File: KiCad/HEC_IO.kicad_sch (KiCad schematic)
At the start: 22 parts, among them SW1 SW_DIP_x04, U12 74LS04, U17 74LS20, U22 74LS02, U30 74LS74, U31 74LS32, U32 LM79M05_TO220, U33 74LS20, U34 74LS393, U35 74LS08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

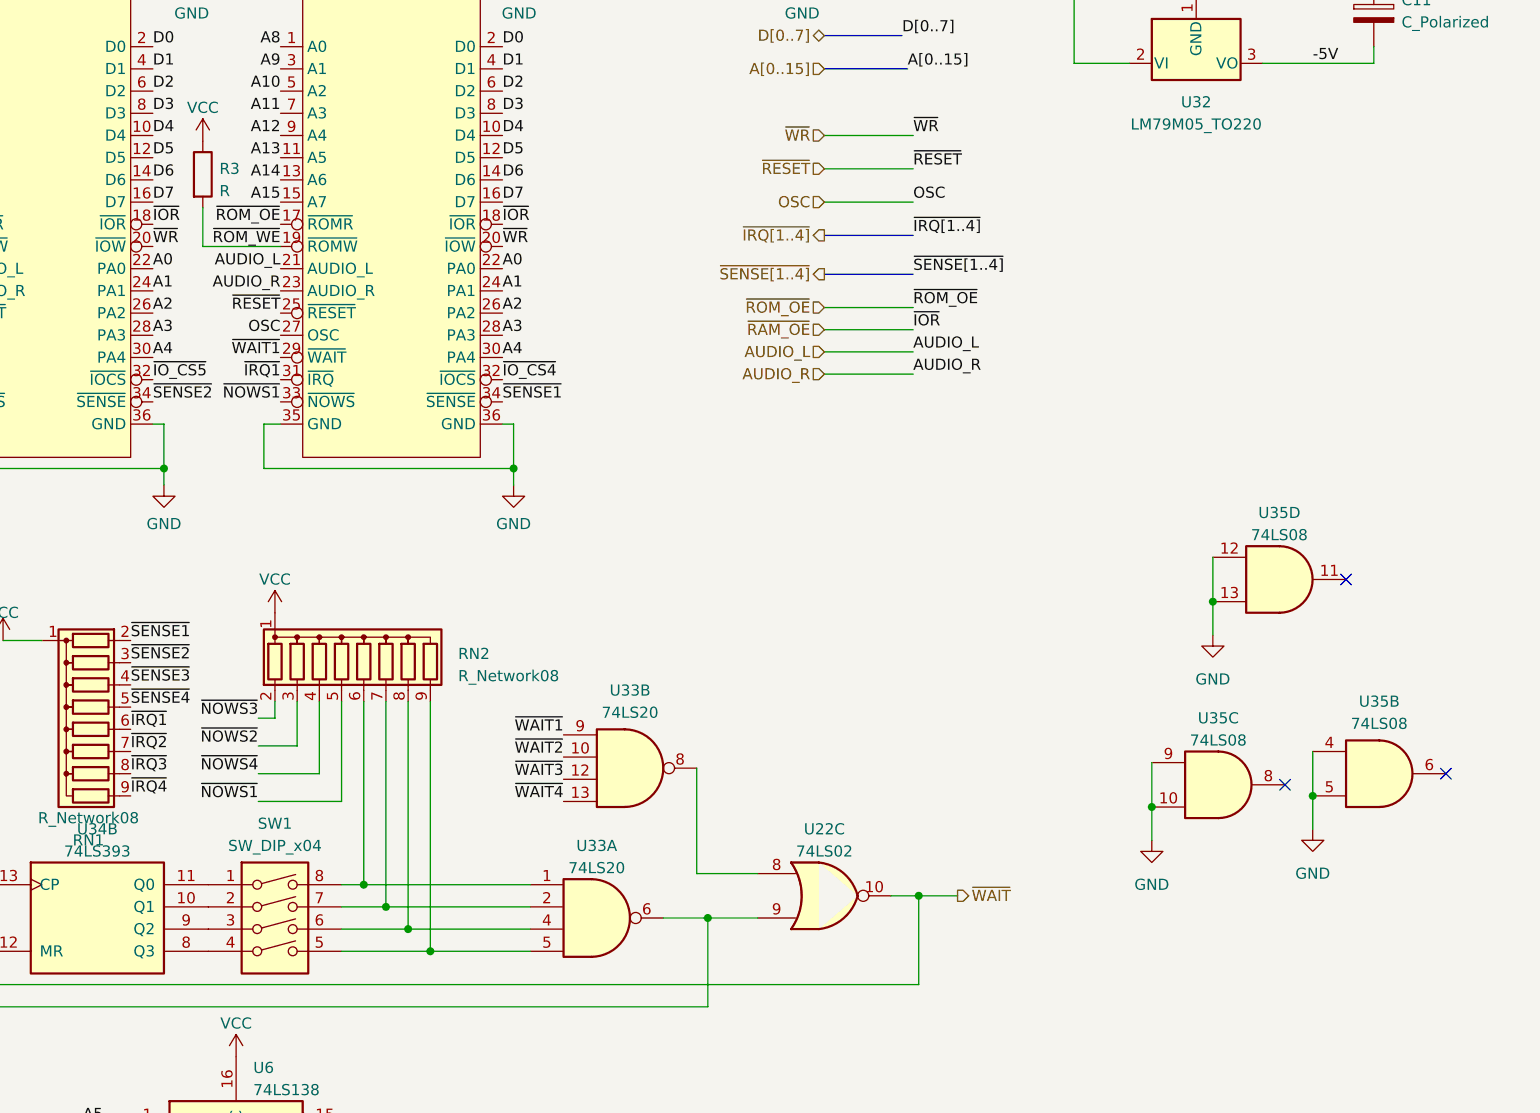
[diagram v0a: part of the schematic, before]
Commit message: Exchange RI and NX pins on bus driver
A mistake is found in the schematic: the RI and NX bits are exchanged on the 74245 bus driver chip. The mistake has been corrected. This change is significant since it changes the (non-existent) software programming model. More playing around with the layout.
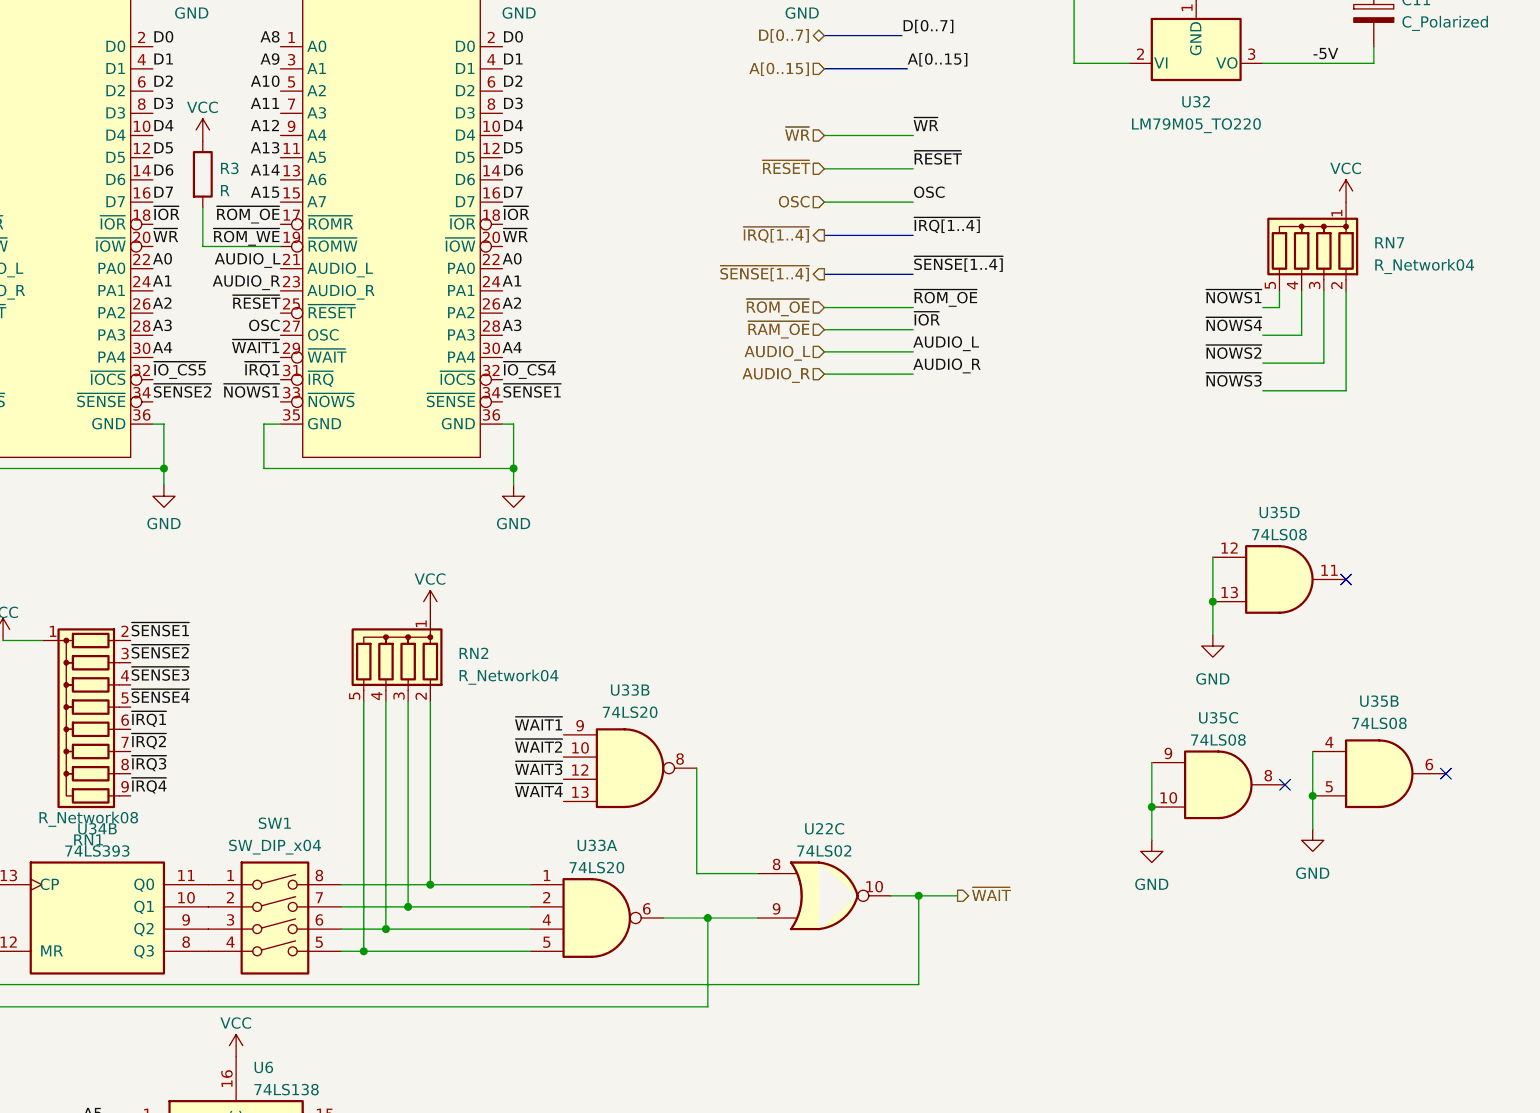
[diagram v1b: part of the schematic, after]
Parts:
- removed RN2: R_Network08, Resistor_THT:R_Array_SIP9, symbol Device:R_Network08
- added RN2, RN7: R_Network04, Resistor_THT:R_Array_SIP5, symbol Device:R_Network04
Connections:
- net VCC: now also RN2.1 (common), RN7.1 (common)
- net ~{NOWS1}: now also RN7.5 (R4)
- net ~{NOWS2}: now also RN7.3 (R2)
- net ~{NOWS3}: now also RN7.2 (R1)
- net ~{NOWS4}: now also RN7.4 (R3)
- net at SW1.5, U33.5: now also RN2.5 (R4)
- net at SW1.6, U33.4: now also RN2.4 (R3)
- net at SW1.7, U33.2: now also RN2.3 (R2)
- net at SW1.8, U33.1: now also RN2.2 (R1)

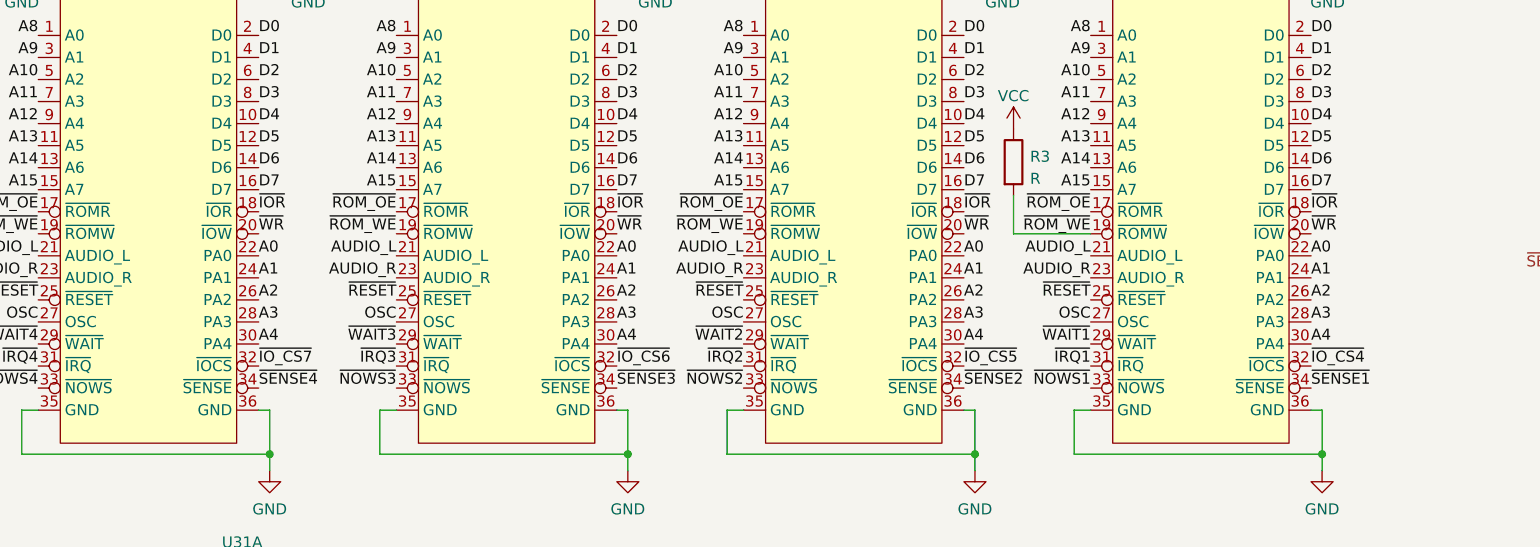
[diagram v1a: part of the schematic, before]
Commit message: Update to bus pinout
Move /RD and /WR signal closer to /CS to simplify add-on card design for common chips. From a simple search of pinouts of common chips this may reduce the amount of vias needed on the card.
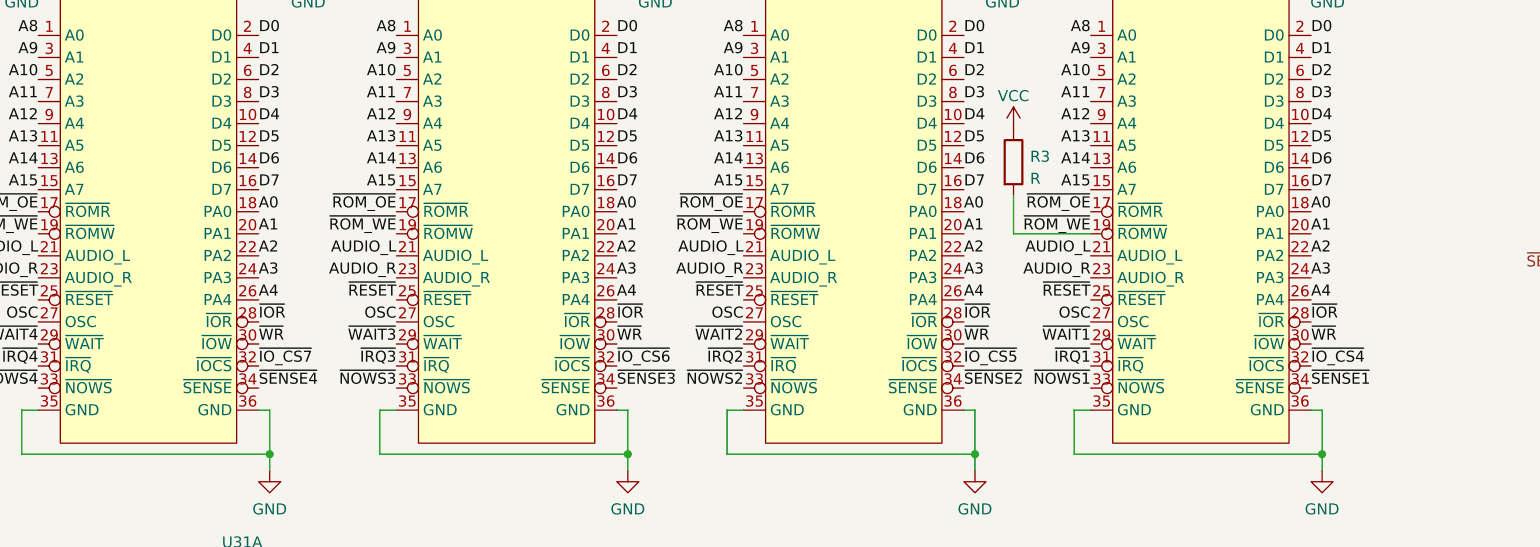
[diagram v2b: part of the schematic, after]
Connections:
- net A0: now also BUS1.18 (PA0), BUS2.18 (PA0), BUS3.18 (PA0), BUS4.18 (PA0); no longer BUS1.22 (PA0), BUS2.22 (PA0), BUS3.22 (PA0), BUS4.22 (PA0)
- net A1: now also BUS1.20 (PA1), BUS2.20 (PA1), BUS3.20 (PA1), BUS4.20 (PA1); no longer BUS1.24 (PA1), BUS2.24 (PA1), BUS3.24 (PA1), BUS4.24 (PA1)
- net A2: now also BUS1.22 (PA2), BUS2.22 (PA2), BUS3.22 (PA2), BUS4.22 (PA2); no longer BUS1.26 (PA2), BUS2.26 (PA2), BUS3.26 (PA2), BUS4.26 (PA2)
- net A3: now also BUS1.24 (PA3), BUS2.24 (PA3), BUS3.24 (PA3), BUS4.24 (PA3); no longer BUS1.28 (PA3), BUS2.28 (PA3), BUS3.28 (PA3), BUS4.28 (PA3)
- net A4: now also BUS1.26 (PA4), BUS2.26 (PA4), BUS3.26 (PA4), BUS4.26 (PA4); no longer BUS1.30 (PA4), BUS2.30 (PA4), BUS3.30 (PA4), BUS4.30 (PA4)
- net ~{RAM_OE}: now also BUS1.28 (~{IOR}), BUS2.28 (~{IOR}), BUS3.28 (~{IOR}), BUS4.28 (~{IOR}); no longer BUS1.18 (~{IOR}), BUS2.18 (~{IOR}), BUS3.18 (~{IOR}), BUS4.18 (~{IOR})
- net ~{WR}: now also BUS1.30 (~{IOW}), BUS2.30 (~{IOW}), BUS3.30 (~{IOW}), BUS4.30 (~{IOW}); no longer BUS1.20 (~{IOW}), BUS2.20 (~{IOW}), BUS3.20 (~{IOW}), BUS4.20 (~{IOW})

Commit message: Bug fixes
fixed some bugs introduced to the schematic. More routing.
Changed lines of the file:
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@@
-    (effects (font (size 1.27 1.27)) (justify right bottom))
-  )
-  (label "~{IORQ}" (at 123.19 181.61 180) (fields_autoplaced)
     (effects (font (size 1.27 1.27)) (justify right bottom))
   )
@@
     (effects (font (size 1.27 1.27)) (justify right))
   )
+  (hierarchical_label "~{IORQ}" (shape input) (at 123.19 181.61 180) (fields_autoplaced)
+    (effects (font (size 1.27 1.27)) (justify right))
+  )

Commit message: Preliminary routing
Changed footprint pad size to allow 2 traces to be routed between adjacent pads. Finished routing all ICs. Bypass caps not added. Some traces may need to be optimized.
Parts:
- U12, U17, U22, U30, U31, U33, U34, U35: footprint Package_DIP:DIP-14_W7.62mm_Socket -> Library:DIP-14_W7.62mm_Socket_ThinPads
- U6: footprint Package_DIP:DIP-16_W7.62mm_Socket -> Library:DIP-16_W7.62mm_Socket_ThinPads
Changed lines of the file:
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@@
       (effects (font (size 1.27 1.27)) (justify left))
     )
-    (property "Footprint" "Package_DIP:DIP-16_W7.62mm_Socket" (at 138.43 173.99 0)
+    (property "Footprint" "Library:DIP-16_W7.62mm_Socket_ThinPads" (at 138.43 173.99 0)
       (effects (font (size 1.27 1.27)) hide)
     )
@@
       (effects (font (size 1.27 1.27)))
     )
-    (property "Footprint" "Package_DIP:DIP-14_W7.62mm_Socket" (at 250.825 127.635 0)
+    (property "Footprint" "Library:DIP-14_W7.62mm_Socket_ThinPads" (at 250.825 127.635 0)
       (effects (font (size 1.27 1.27)) hide)
     )
@@
       (effects (font (size 1.27 1.27)) (justify left))
     )
-    (property "Footprint" "Package_DIP:DIP-14_W7.62mm_Socket" (at 20.955 176.53 0)
+    (property "Footprint" "Library:DIP-14_W7.62mm_Socket_ThinPads" (at 20.955 176.53 0)
       (effects (font (size 1.27 1.27)) hide)
     )
@@
       (effects (font (size 1.27 1.27)))
     )
-    (property "Footprint" "Package_DIP:DIP-14_W7.62mm_Socket" (at 76.2 135.255 0)
+    (property "Footprint" "Library:DIP-14_W7.62mm_Socket_ThinPads" (at 76.2 135.255 0)
       (effects (font (size 1.27 1.27)) hide)
     )
@@
       (effects (font (size 1.27 1.27)))
     )
-    (property "Footprint" "Package_DIP:DIP-14_W7.62mm_Socket" (at 205.74 140.335 0)
+    (property "Footprint" "Library:DIP-14_W7.62mm_Socket_ThinPads" (at 205.74 140.335 0)
       (effects (font (size 1.27 1.27)) hide)
     )
@@
       (effects (font (size 1.27 1.27)))
     )
-    (property "Footprint" "Package_DIP:DIP-14_W7.62mm_Socket" (at 84.455 146.05 0)
+    (property "Footprint" "Library:DIP-14_W7.62mm_Socket_ThinPads" (at 84.455 146.05 0)
       (effects (font (size 1.27 1.27)) hide)
     )
@@
       (effects (font (size 1.27 1.27)))
     )
-    (property "Footprint" "Package_DIP:DIP-14_W7.62mm_Socket" (at 45.72 109.22 0)
+    (property "Footprint" "Library:DIP-14_W7.62mm_Socket_ThinPads" (at 45.72 109.22 0)
       (effects (font (size 1.27 1.27)) hide)
     )
@@
       (effects (font (size 1.27 1.27)))
     )
-    (property "Footprint" "Package_DIP:DIP-14_W7.62mm_Socket" (at 257.81 104.14 0)
+    (property "Footprint" "Library:DIP-14_W7.62mm_Socket_ThinPads" (at 257.81 104.14 0)
       (effects (font (size 1.27 1.27)) hide)
     )
@@
       (effects (font (size 1.27 1.27)))
     )
-    (property "Footprint" "Package_DIP:DIP-14_W7.62mm_Socket" (at 269.24 126.365 0)
+    (property "Footprint" "Library:DIP-14_W7.62mm_Socket_ThinPads" (at 269.24 126.365 0)
       (effects (font (size 1.27 1.27)) hide)
     )
@@
       (effects (font (size 1.27 1.27)))
     )
-    (property "Footprint" "Package_DIP:DIP-14_W7.62mm_Socket" (at 179.705 142.875 0)
+    (property "Footprint" "Library:DIP-14_W7.62mm_Socket_ThinPads" (at 179.705 142.875 0)
       (effects (font (size 1.27 1.27)) hide)
     )
@@
       (effects (font (size 1.27 1.27)) (justify left))
     )
-    (property "Footprint" "Package_DIP:DIP-14_W7.62mm_Socket" (at 41.275 176.53 0)
+    (property "Footprint" "Library:DIP-14_W7.62mm_Socket_ThinPads" (at 41.275 176.53 0)
       (effects (font (size 1.27 1.27)) hide)
     )
@@
       (effects (font (size 1.27 1.27)))
     )
-    (property "Footprint" "Package_DIP:DIP-14_W7.62mm_Socket" (at 27.305 139.065 0)
+    (property "Footprint" "Library:DIP-14_W7.62mm_Socket_ThinPads" (at 27.305 139.065 0)
       (effects (font (size 1.27 1.27)) hide)
     )
@@
       (effects (font (size 1.27 1.27)) (justify left))
     )
-    (property "Footprint" "Package_DIP:DIP-14_W7.62mm_Socket" (at 93.98 135.255 0)
+    (property "Footprint" "Library:DIP-14_W7.62mm_Socket_ThinPads" (at 93.98 135.255 0)
       (effects (font (size 1.27 1.27)) hide)
     )
@@
       (effects (font (size 1.27 1.27)))
     )
-    (property "Footprint" "Package_DIP:DIP-14_W7.62mm_Socket" (at 27.305 125.73 0)
+    (property "Footprint" "Library:DIP-14_W7.62mm_Socket_ThinPads" (at 27.305 125.73 0)
       (effects (font (size 1.27 1.27)) hide)
     )
@@
       (effects (font (size 1.27 1.27)))
     )
-    (property "Footprint" "Package_DIP:DIP-14_W7.62mm_Socket" (at 27.305 153.035 0)
+    (property "Footprint" "Library:DIP-14_W7.62mm_Socket_ThinPads" (at 27.305 153.035 0)
       (effects (font (size 1.27 1.27)) hide)
     )
@@
       (effects (font (size 1.27 1.27)))
     )
-    (property "Footprint" "Package_DIP:DIP-14_W7.62mm_Socket" (at 45.72 150.495 0)
+    (property "Footprint" "Library:DIP-14_W7.62mm_Socket_ThinPads" (at 45.72 150.495 0)
       (effects (font (size 1.27 1.27)) hide)
     )
@@
       (effects (font (size 1.27 1.27)) (justify left))
     )
-    (property "Footprint" "Package_DIP:DIP-14_W7.62mm_Socket" (at 81.915 176.53 0)
+    (property "Footprint" "Library:DIP-14_W7.62mm_Socket_ThinPads" (at 81.915 176.53 0)
       (effects (font (size 1.27 1.27)) hide)
     )
@@
       (effects (font (size 1.27 1.27)))
     )
-    (property "Footprint" "Package_DIP:DIP-14_W7.62mm_Socket" (at 45.72 123.19 0)
+    (property "Footprint" "Library:DIP-14_W7.62mm_Socket_ThinPads" (at 45.72 123.19 0)
       (effects (font (size 1.27 1.27)) hide)
     )
@@
       (effects (font (size 1.27 1.27)))
     )
-    (property "Footprint" "Package_DIP:DIP-14_W7.62mm_Socket" (at 183.515 125.73 0)
+    (property "Footprint" "Library:DIP-14_W7.62mm_Socket_ThinPads" (at 183.515 125.73 0)
       (effects (font (size 1.27 1.27)) hide)
     )
@@
       (effects (font (size 1.27 1.27)))
     )
-    (property "Footprint" "Package_DIP:DIP-14_W7.62mm_Socket" (at 122.555 141.605 0)
+    (property "Footprint" "Library:DIP-14_W7.62mm_Socket_ThinPads" (at 122.555 141.605 0)
       (effects (font (size 1.27 1.27)) hide)
     )
@@
       (effects (font (size 1.27 1.27)))
     )
-    (property "Footprint" "Package_DIP:DIP-14_W7.62mm_Socket" (at 45.72 136.525 0)
+    (property "Footprint" "Library:DIP-14_W7.62mm_Socket_ThinPads" (at 45.72 136.525 0)
       (effects (font (size 1.27 1.27)) hide)
     )
@@
       (effects (font (size 1.27 1.27)) (justify left))
     )
-    (property "Footprint" "Package_DIP:DIP-14_W7.62mm_Socket" (at 62.23 176.53 0)
+    (property "Footprint" "Library:DIP-14_W7.62mm_Socket_ThinPads" (at 62.23 176.53 0)
       (effects (font (size 1.27 1.27)) hide)
     )
@@
       (effects (font (size 1.27 1.27)))
     )
-    (property "Footprint" "Package_DIP:DIP-14_W7.62mm_Socket" (at 27.305 111.76 0)
+    (property "Footprint" "Library:DIP-14_W7.62mm_Socket_ThinPads" (at 27.305 111.76 0)
       (effects (font (size 1.27 1.27)) hide)
     )
@@
       (effects (font (size 1.27 1.27)) (justify left))
     )
-    (property "Footprint" "Package_DIP:DIP-14_W7.62mm_Socket" (at 102.235 176.53 0)
-      (effects (font (size 1.27 1.27)) hide)
-    )
+    (property "Footprint" "Library:DIP-14_W7.62mm_Socket_ThinPads" (at 102.235 176.53 0)
+      (effects (font (size 1.27 1.27)) hide)
+    )

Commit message: fix DRC errors, generate gerbers
Fixed all DRC errors (except a few silkscreen clipped warnings). Generated gerber files for first version of the board.
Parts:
- U32: footprint Package_TO_SOT_THT:TO-92_Inline -> Package_TO_SOT_THT:TO-220-3_Vertical
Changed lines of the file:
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@@
       (effects (font (size 1.27 1.27)))
     )
-    (property "Footprint" "Package_TO_SOT_THT:TO-92_Inline" (at 248.285 50.165 0)
+    (property "Footprint" "Package_TO_SOT_THT:TO-220-3_Vertical" (at 248.285 50.165 0)
       (effects (font (size 1.27 1.27) italic) hide)
     )
